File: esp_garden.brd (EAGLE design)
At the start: 50 x 100 mm, 31 parts, among them T1 DMN6068SE-13, T2 DMN6068SE-13, T3 DMN6068SE-13, T4 DMN6068SE-13, U1 V1, U10 V1, U11 V1, U12 V1, U13 V1, U14 V1, U15 V1, U2 V1, U3 V1, U4 V1, U5 V1, U6 V1, U7 V1, U8 V1, U9 V1

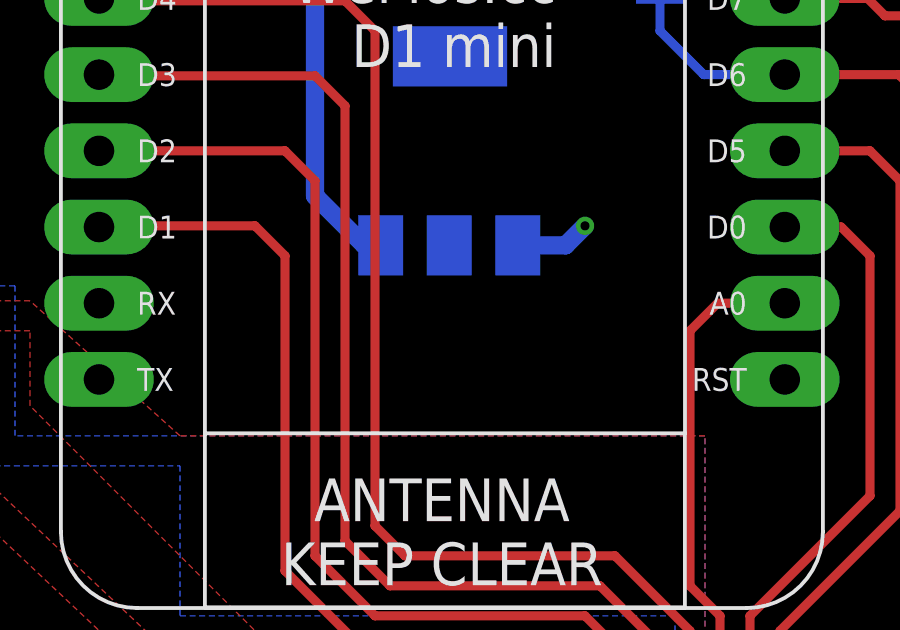
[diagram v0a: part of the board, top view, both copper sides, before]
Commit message: Isolate for planes set to 0.254, added caps at LDO
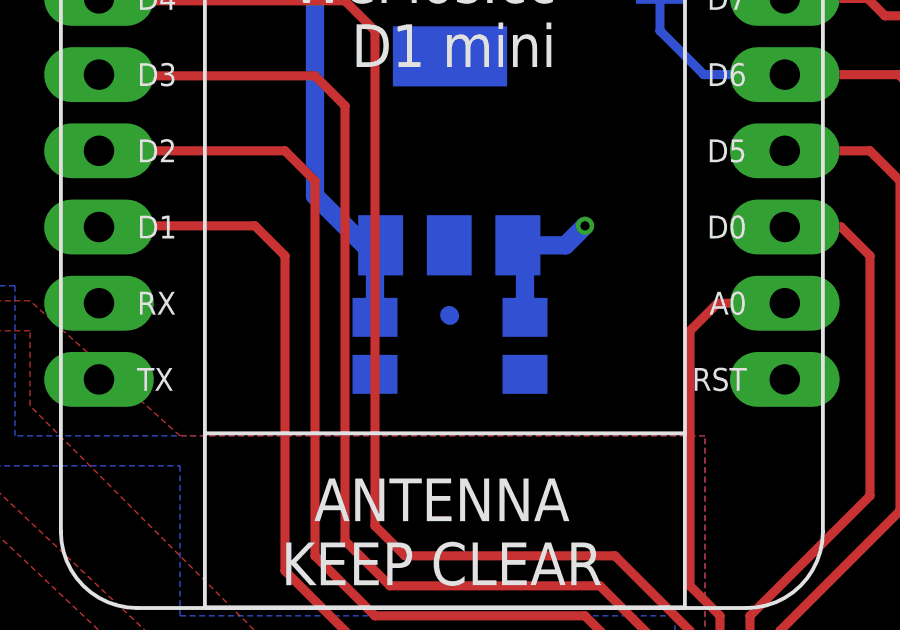
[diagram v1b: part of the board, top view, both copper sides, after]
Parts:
- added C1, C2: (no value), rcl:C0805
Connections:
- net +12V: now also C1.1
- net +3V3: now also C2.1
- net GND: now also C1.2, C2.2
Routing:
- net +3V3: track 8.70 -> 11.2 mm
- net +12V: track 37.8 -> 40.2 mm
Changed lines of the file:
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@@
 <grid distance="0.5" unitdist="mm" unit="mm" style="lines" multiple="1" display="no" altdistance="0.025" altunitdist="inch" altunit="mm"/>
 <layers>
-<layer number="1" name="Top" color="4" fill="1" visible="yes" active="yes"/>
+<layer number="1" name="Top" color="4" fill="1" visible="no" active="yes"/>
 <layer number="2" name="Route2" color="1" fill="3" visible="no" active="no"/>
 <layer number="3" name="Route3" color="4" fill="3" visible="no" active="no"/>
@@
 <element name="D5" library="diode" package="SMB" value="ES2D" x="20.3" y="91.1" rot="MR0"/>
 <element name="U15" library="JKW_CHIP" package="2_SCREW_PIN" value="V1" x="45" y="88" rot="R90"/>
+<element name="C1" library="rcl" package="C0805" value="" x="22.5" y="74.5" rot="MR270"/>
+<element name="C2" library="rcl" package="C0805" value="" x="27.5" y="74.5" rot="MR270"/>
 </elements>
 <signals>
@@
 <contactref element="U12" pad="P$1"/>
 <contactref element="U14" pad="P$2"/>
-<polygon width="0.6096" layer="16">
+<polygon width="0.6096" layer="16" isolate="0.254">
 <vertex x="6" y="99.5"/>
 <vertex x="49.5" y="99.5"/>
@@
 </polygon>
 <wire x1="5.5" y1="85.5" x2="7.5" y2="85.5" width="1.27" layer="16"/>
+<contactref element="C1" pad="2"/>
+<contactref element="C2" pad="2"/>
+<wire x1="24.9746" y1="75.5254" x2="25" y2="75.5" width="0.6096" layer="16"/>
 </signal>
 <signal name="RELAY_L_3">
@@
 <wire x1="21" y1="94" x2="22.5" y2="92.5" width="0.6096" layer="16"/>
 <wire x1="22.5" y1="92.5" x2="22.5" y2="91.1" width="0.6096" layer="16"/>
-<polygon width="0.6096" layer="16">
+<polygon width="0.6096" layer="16" isolate="0.254">
 <vertex x="0.5" y="99.5"/>
 <vertex x="5" y="99.5"/>
@@
 </polygon>
 <wire x1="5.5" y1="90.5" x2="3.5" y2="90.5" width="1.27" layer="16"/>
+<contactref element="C1" pad="1"/>
+<wire x1="22.5" y1="75.45" x2="22.5" y2="77.6618" width="0.6096" layer="16"/>
+<wire x1="22.5" y1="77.6618" x2="22.6886" y2="77.8504" width="0.6096" layer="16"/>
 </signal>
 <signal name="+3V3">
@@
 <wire x1="28.8504" y1="77.8504" x2="29.5" y2="78.5" width="0.6096" layer="16"/>
 <via x="29.5" y="78.5" extent="1-16" drill="0.3048"/>
-<polygon width="0.6096" layer="1">
+<polygon width="0.6096" layer="1" isolate="0.254">
 <vertex x="0.5" y="99.5"/>
 <vertex x="49.5" y="99.5"/>
@@
 <vertex x="0.5" y="76"/>
 </polygon>
+<contactref element="C2" pad="1"/>
+<wire x1="27.5" y1="75.45" x2="27.5" y2="77.611" width="0.6096" layer="16"/>
+<wire x1="27.5" y1="77.611" x2="27.2606" y2="77.8504" width="0.6096" layer="16"/>
 </signal>
 <signal name="RELAY_0">
@@
 <contactref element="RELAY2" pad="SWCOMMON"/>
 <contactref element="RELAY3" pad="SWCOMMON"/>
-<polygon width="0.6096" layer="1">
+<polygon width="0.6096" layer="1" isolate="0.254">
 <vertex x="0.5" y="71"/>
 <vertex x="8.5" y="71"/>
@@
 <contactref element="U3" pad="P$2"/>
 <contactref element="U4" pad="P$2"/>
-<polygon width="0.6096" layer="1">
+<polygon width="0.6096" layer="1" isolate="0.254">
 <vertex x="0.5" y="70"/>
 <vertex x="8" y="70"/>

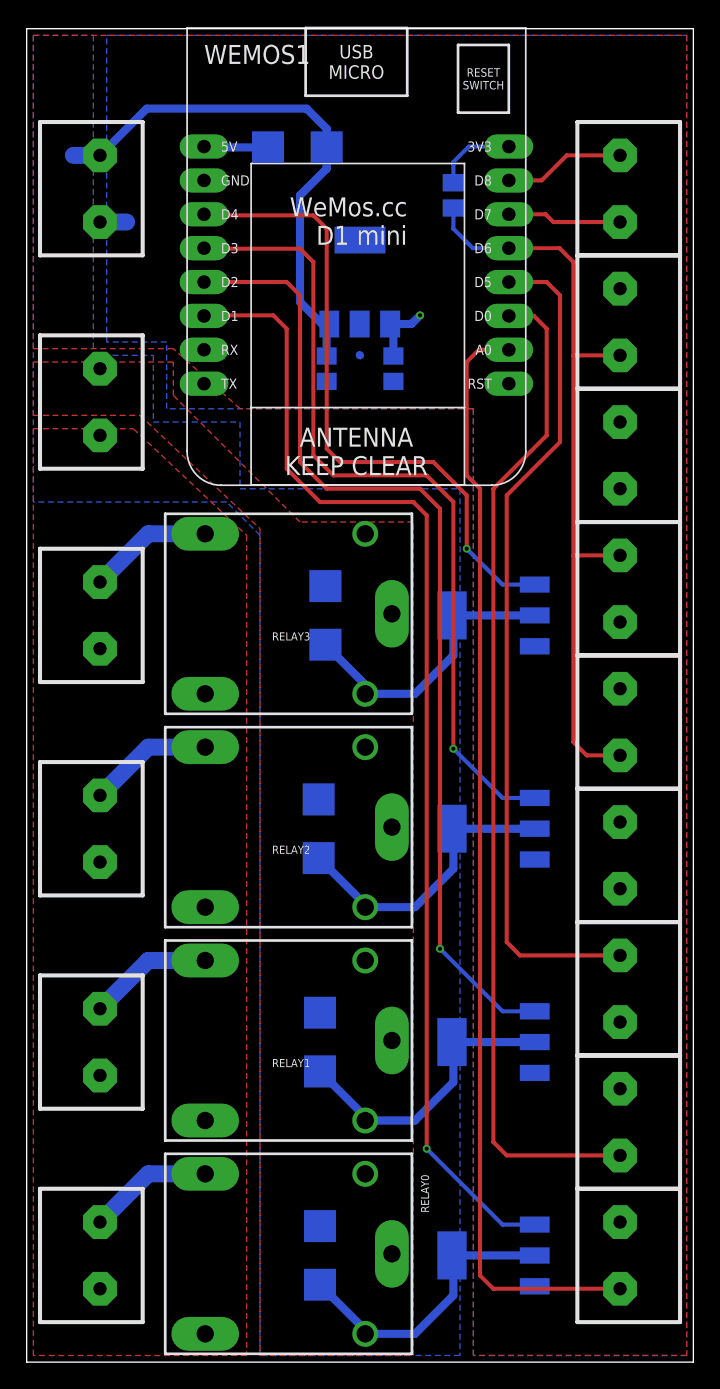
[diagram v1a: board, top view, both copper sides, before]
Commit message: Added support for I2C sensor, changed LDO to REG1117
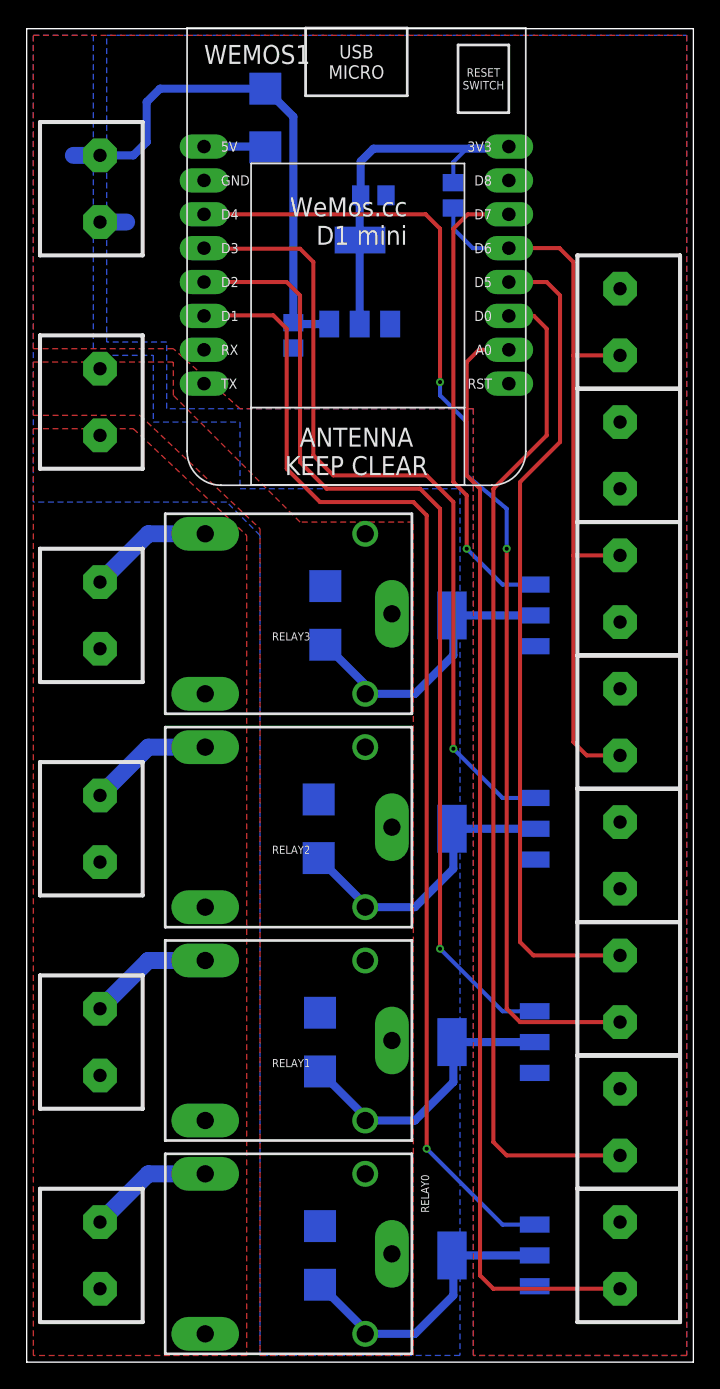
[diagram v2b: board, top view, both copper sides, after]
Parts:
- removed U13: V1, JKW_CHIP:2_SCREW_PIN
- IC1: value REG1118 -> REG1117
- moved U15 60.0 mm to (45.0, 28.0)
- moved C2 13.1 mm to (26.0, 87.5), turned to 180 degrees
- moved U12 10.0 mm to (45.0, 18.0)
- moved C1 3.54 mm to (20.0, 77.0)
- moved D5 3.26 mm to (17.9, 93.3), turned to 270 degrees
- renumbered LDO to IC1
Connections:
- removed net D7: U15.P$1, WEMOS1.D7
- removed net DHT: U12.P$2, WEMOS1.D5
- new net SCL: U15.P$2, WEMOS1.D5
- new net SDA/DHT: U15.P$1, WEMOS1.D4
- net +3V3: now also IC1.2; no longer IC1.1, U13.P$2
- net D8: no longer U15.P$2
- net GND: now also IC1.1, U12.P$2; no longer IC1.2, U12.P$1
- net HUMIDITY_P: now also U12.P$1; no longer U13.P$1
- net RELAY_3: now also WEMOS1.D7; no longer WEMOS1.D4
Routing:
- net SDA/DHT: track 0.00 -> 87.8 mm, vias 0 -> 2
- net DHT: track 63.3 -> 0.00 mm
- net SCL: track 0.00 -> 61.9 mm
- net +3V3: track 11.2 -> 30.0 mm, vias 1 -> 0
- net RELAY_3: track 48.3 -> 35.2 mm
- net D8: track 9.12 -> 0.00 mm
- net D7: track 8.58 -> 0.00 mm
- net +12V: track 40.2 -> 42.1 mm

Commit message: Added text on PCB
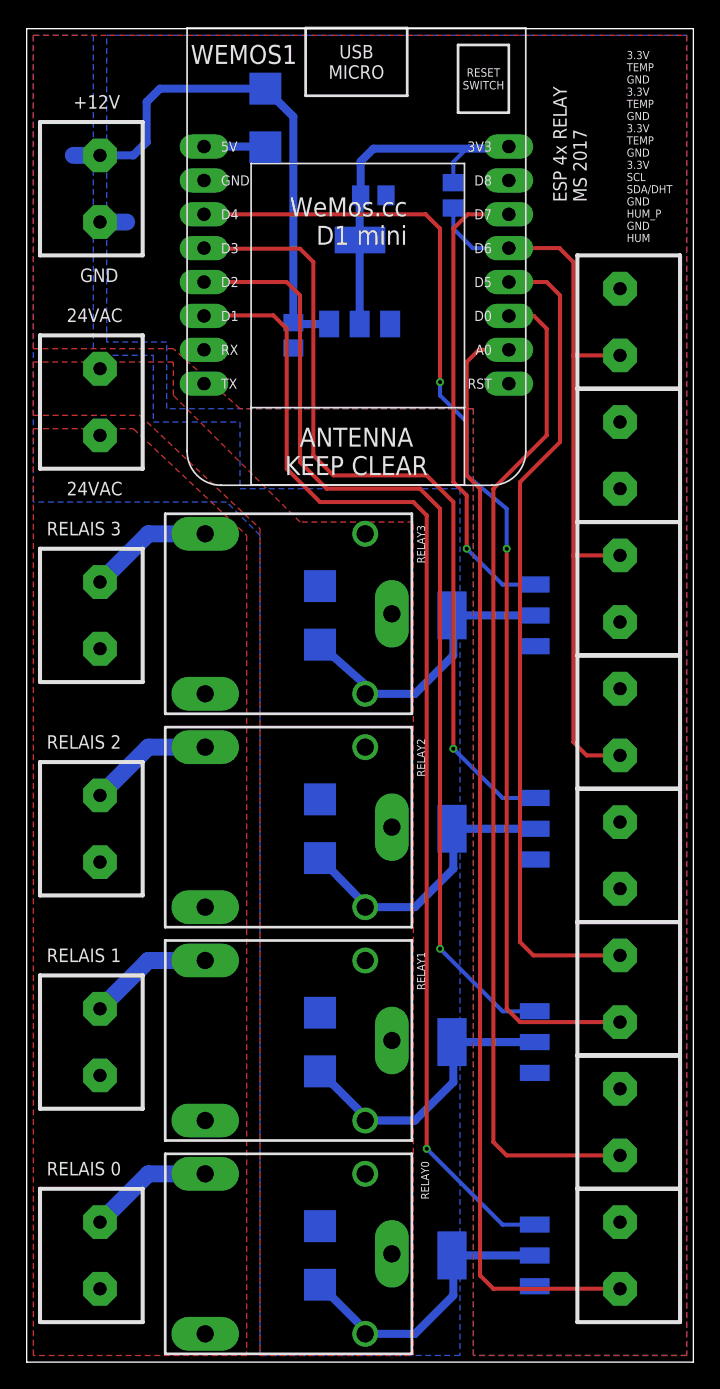
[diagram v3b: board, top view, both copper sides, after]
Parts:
- added U$1: LOGO_NO_TRASHNO_TRASH, JKW_CHIP:LOGO_ROHS_NO_TRASH
- moved D4 0.40 mm to (22.0, 56.0)
- moved D3 0.10 mm to (22.0, 40.0)
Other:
- board text added: "+12V"
- board text added: "24VAC"
- board text added: "3.3V"
- board text added: "3.3V TEMP GND 3.3V TEMP GND 3.3V TEMP GND 3.3V SCL SDA/DHT GND HUM_P GND HUM"
- board text added: "ESP 4x RELAY"
- board text added: "GND"
- board text added: "HUM"
- board text added: "HUM_P"
- board text added: "MS 2017"
- board text added: "RELAIS 0"
- board text added: "RELAIS 1"
- board text added: "RELAIS 2"
- board text added: "RELAIS 3"
- board text added: "SCL"
- board text added: "SDA"
- board text added: "TEMP"
